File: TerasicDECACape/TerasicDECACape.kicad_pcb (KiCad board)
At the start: 4 copper layers, 54.7 x 66.3 mm, 24 parts, among them CN1 NASB0-S6701-TS50, CN2 NASB0-S6701-TS50, J1 MiSTer SDRAM Module, J2 USB_A, J3 Conn_01x03_Male, M1 Sipeed Lichee, P8 BeagleBone_Black_Header, P9 BeagleBone_Black_Header, SW1 TS-1187A-B-A-B, SW2 TS-1187A-B-A-B

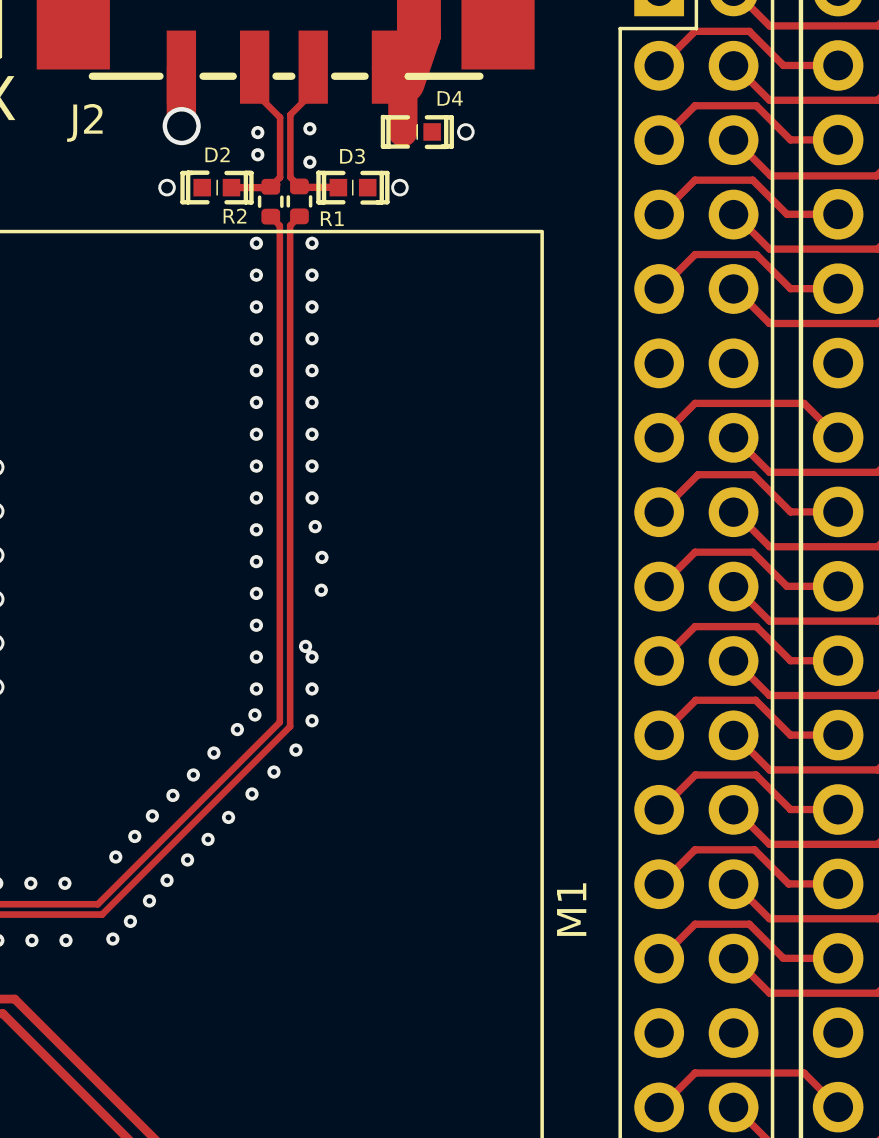
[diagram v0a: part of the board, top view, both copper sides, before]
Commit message: add mounting hole for module
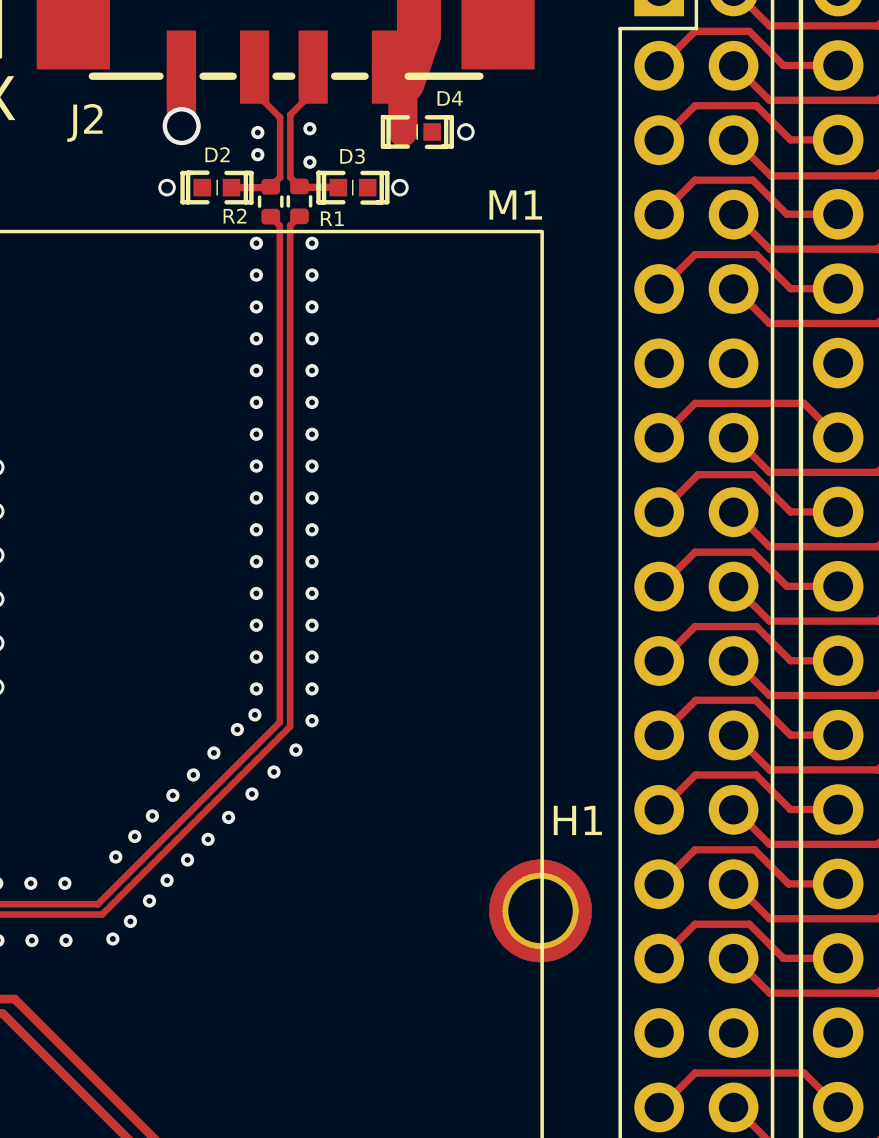
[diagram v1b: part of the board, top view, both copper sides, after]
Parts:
- added H1: MountingHole_Pad, MountingHole:MountingHole_2.2mm_M2_ISO7380_Pad_TopBottom, F.Cu at (154.5, 96.3)
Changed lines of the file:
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@@
     (fp_line (start -2.27 -0.94) (end -2.27 0.94) (layer "F.SilkS") (width 0.15))
     (fp_arc (start 0.001269 0.002199) (mid -0.112199 -0.418731) (end 0 -0.84) (layer "F.SilkS") (width 0.08))
-    (fp_arc (start -0.001269 -0.002199) (mid 0.112199 0.418731) (end 0 0.84) (layer "F.SilkS") (width 0.08))
+    (fp_arc (start -0.001269 -0.002199) (mid 0.112199 0.41873) (end 0 0.84) (layer "F.SilkS") (width 0.08))
     (fp_circle (center -1.6 0.8) (end -1.57 0.8) (layer "F.Fab") (width 0.06) (fill none))
     (pad "1" smd rect locked (at -1.45 0 180) (size 1.19 1.73) (layers "F.Cu" "F.Paste" "F.Mask")
@@
     )
   )
+  (footprint "MountingHole:MountingHole_2.2mm_M2_ISO7380_Pad_TopBottom" (layer "F.Cu")
+    (at 154.4701 96.3224)
+    (descr "Mounting Hole 2.2mm, M2, ISO7380")
+    (tags "mounting hole 2.2mm m2 iso7380")
+    (property "Sheetfile" "TerasicDECACape.kicad_sch")
+    (property "Sheetname" "")
+    (attr exclude_from_pos_files)
+    (fp_text reference "H1" (at 1.27 -3.05) (layer "F.SilkS")
+      (effects (font (size 1 1) (thickness 0.15)))
+    )
+    (fp_text value "MountingHole_Pad" (at 0 2.75) (layer "F.Fab")
+      (effects (font (size 1 1) (thickness 0.15)))
+    )
+    (fp_text user "${REFERENCE}" (at 0 0) (layer "F.Fab")
+      (effects (font (size 1 1) (thickness 0.15)))
+    )
+    (fp_circle (center 0 0) (end 1.75 0) (layer "Cmts.User") (width 0.15) (fill none))
+    (fp_circle (center 0 0) (end 2 0) (layer "F.CrtYd") (width 0.05) (fill none))
+    (pad "1" connect circle (at 0 0) (size 3.5 3.5) (layers "B.Cu" "B.Mask")
+      (net 1 "GND") (pinfunction "1") (pintype "input"))
+    (pad "1" thru_hole circle (at 0 0) (size 2.6 2.6) (drill 2.2) (layers *.Cu *.Mask)
+      (net 1 "GND") (pinfunction "1") (pintype "input"))
+    (pad "1" connect circle (at 0 0) (size 3.5 3.5) (layers "F.Cu" "F.Mask")
+      (net 1 "GND") (pinfunction "1") (pintype "input"))
+  )
   (footprint "easyeda2kicad:Sipeed Lichee" (layer "F.Cu")
     (at 154.5251 96.2324 90)
-    (fp_text reference "M1" (at -0.05 1.045 90 unlocked) (layer "F.SilkS")
+    (fp_text reference "M1" (at 23.97 -0.905 unlocked) (layer "F.SilkS")
       (effects (font (size 1 1) (thickness 0.15)))
     )
@@
   (gr_text "TX" (at 135.2701 68.6324) (layer "F.SilkS")
     (effects (font (size 1.5 1.5) (thickness 0.3)))
+  )
+  (dimension (type aligned) (layer "Dwgs.User")
+    (pts (xy 127.5801 95.0924) (xy 127.5801 96.2624))
+    (height -24.64)
+    (gr_text "1.1700 mm" (at 151.5951 95.6774 90) (layer "Dwgs.User")
+      (effects (font (size 0.5 0.5) (thickness 0.15)))
+    )
+    (format (units 3) (units_format 1) (precision 4))
+    (style (thickness 0.1) (arrow_length 0.5) (text_position_mode 0) (extension_height 0.58642) (extension_offset 0.5) keep_text_aligned)
   )
   (segment (start 126.8501 98.7024) (end 127.5701 97.9824) (width 0.25) (layer "F.Cu") (net 1))
@@
   (via (at 139.8701 97.2824) (size 0.45) (drill 0.2) (layers "F.Cu" "B.Cu") (free) (net 1))
   (via (at 144.7701 88.745724) (size 0.45) (drill 0.2) (layers "F.Cu" "B.Cu") (free) (net 1))
-  (via (at 146.987292 85.375398) (size 0.45) (drill 0.2) (layers "F.Cu" "B.Cu") (free) (net 1))
+  (via (at 146.6701 85.485726) (size 0.45) (drill 0.2) (layers "F.Cu" "B.Cu") (free) (net 1))
   (via (at 124.0701 104.81365) (size 0.45) (drill 0.2) (layers "F.Cu" "B.Cu") (free) (net 1))
   (via (at 144.7701 74.619066) (size 0.45) (drill 0.2) (layers "F.Cu" "B.Cu") (free) (net 1))
@@
   (via (at 124.0701 102.2074) (size 0.45) (drill 0.2) (layers "F.Cu" "B.Cu") (free) (net 1))
   (via (at 141.7201 71.6324) (size 0.6) (drill 0.4) (layers "F.Cu" "B.Cu") (free) (net 1))
-  (via (at 146.449191 87.293844) (size 0.45) (drill 0.2) (layers "F.Cu" "B.Cu") (free) (net 1))
+  (via (at 146.6701 86.572392) (size 0.45) (drill 0.2) (layers "F.Cu" "B.Cu") (free) (net 1))
   (via (at 138.2701 97.3324) (size 0.45) (drill 0.2) (layers "F.Cu" "B.Cu") (free) (net 1))
   (via (at 141.2201 93.0824) (size 0.45) (drill 0.2) (layers "F.Cu" "B.Cu") (free) (net 1))
@@
   (via (at 146.6701 82.225728) (size 0.45) (drill 0.2) (layers "F.Cu" "B.Cu") (free) (net 1))
   (via (at 128.5201 103.5824) (size 0.6) (drill 0.4) (layers "F.Cu" "B.Cu") (net 1))
-  (via (at 146.777194 83.2053) (size 0.45) (drill 0.2) (layers "F.Cu" "B.Cu") (free) (net 1))
+  (via (at 146.6701 83.312394) (size 0.45) (drill 0.2) (layers "F.Cu" "B.Cu") (free) (net 1))
   (via (at 130.1701 118.6824) (size 1.5) (drill 1.2) (layers "F.Cu" "B.Cu") (net 1))
   (via (at 122.2701 105.3824) (size 0.45) (drill 0.2) (layers "F.Cu" "B.Cu") (free) (net 1))
@@
   (via (at 144.7701 81.139062) (size 0.45) (drill 0.2) (layers "F.Cu" "B.Cu") (free) (net 1))
   (via (at 143.1201 93.8824) (size 0.45) (drill 0.2) (layers "F.Cu" "B.Cu") (free) (net 1))
-  (via (at 147.00778 84.255886) (size 0.45) (drill 0.2) (layers "F.Cu" "B.Cu") (free) (net 1))
+  (via (at 146.6701 84.39906) (size 0.45) (drill 0.2) (layers "F.Cu" "B.Cu") (free) (net 1))
   (via (at 122.2701 102.3074) (size 0.45) (drill 0.2) (layers "F.Cu" "B.Cu") (free) (net 1))
   (via (at 122.7201 97.3824) (size 0.45) (drill 0.2) (layers "F.Cu" "B.Cu") (free) (net 1))
@@
   (segment (start 145.5791 69.2394) (end 144.7101 68.3704) (width 0.225) (layer "F.Cu") (net 180))
   (segment (start 145.5791 71.2834) (end 145.5791 69.2394) (width 0.225) (layer "F.Cu") (net 180))
-  (segment (start 145.1701 71.6224) (end 145.3801 71.6224) (width 0.25) (layer "F.Cu") (net 180))
   (segment (start 143.9201 71.6324) (end 145.1601 71.6324) (width 0.25) (layer "F.Cu") (net 180))
   (segment (start 144.7101 68.2824) (end 144.7101 67.5199) (width 0.25) (layer "F.Cu") (net 180))
-  (segment (start 145.3801 71.6224) (end 145.4701 71.5324) (width 0.25) (layer "F.Cu") (net 180))
   (segment (start 144.7101 68.3704) (end 144.7101 67.5199) (width 0.225) (layer "F.Cu") (net 180))
   (segment (start 146.3201 71.6224) (end 147.5601 71.6224) (width 0.25) (layer "F.Cu") (net 181))
   (segment (start 146.7101 68.3424) (end 146.7101 67.5199) (width 0.25) (layer "F.Cu") (net 181))
-  (segment (start 146.1801 71.6224) (end 146.1201 71.6824) (width 0.25) (layer "F.Cu") (net 181))
   (segment (start 146.7101 68.3024) (end 146.7101 67.5199) (width 0.25) (layer "F.Cu") (net 181))
   (segment (start 146.3201 71.6224) (end 146.1801 71.6224) (width 0.25) (layer "F.Cu") (net 181))

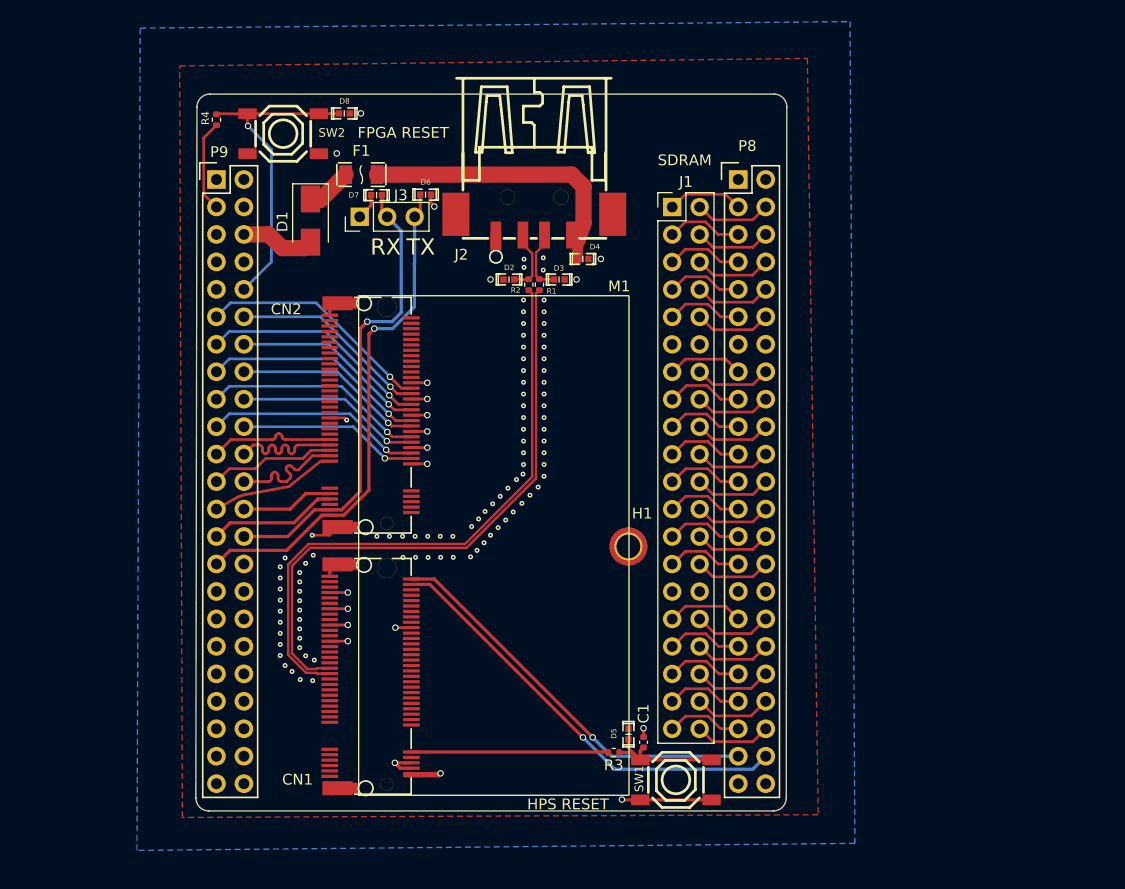
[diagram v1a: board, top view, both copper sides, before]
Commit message: add user IO header, connect UART1 with flow control
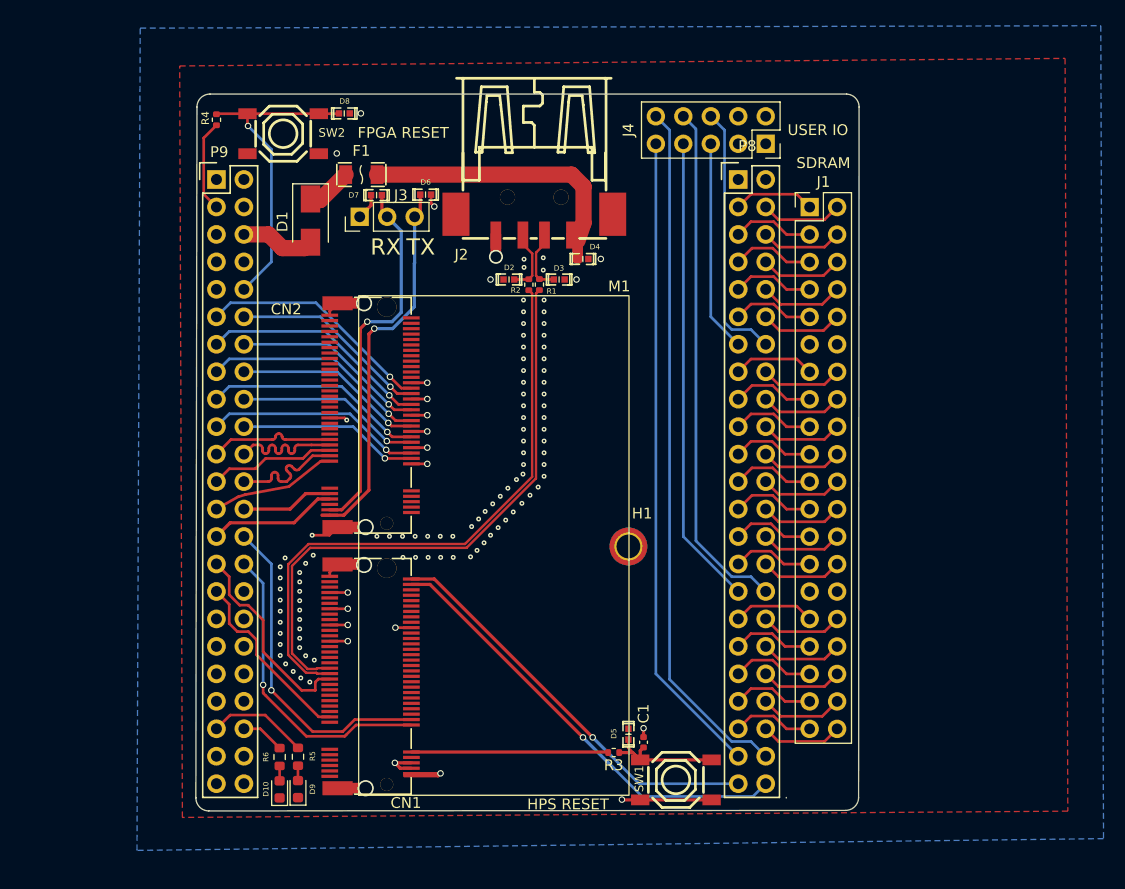
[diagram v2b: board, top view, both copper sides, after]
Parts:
- added D10: red, LED_SMD:LED_0603_1608Metric, F.Cu at (122.2, 118.8)
- added D9: blue, LED_SMD:LED_0603_1608Metric, F.Cu at (123.9, 118.8)
- added J4: Conn_02x05_Odd_Even, Connector_PinSocket_2.54mm:PinSocket_2x05_P2.54mm_Vertical, F.Cu at (167.2, 59.1)
- added R5: 1k, Resistor_SMD:R_0603_1608Metric, F.Cu at (123.9, 115.8)
- added R6: 1k, Resistor_SMD:R_0603_1608Metric, F.Cu at (122.2, 115.8)
- moved J1 12.7 mm to (171.2, 64.9)
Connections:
- CN1 pad 20: /PG8 -> /PG8_UART1_RTS
- CN1 pad 22: /PG9 -> /PG9_UART1_CTS
- CN1 pad 23: /PG7 -> /PG7_UART1_RX
- CN1 pad 37: /PG6 -> /PG6_UART1_TX
- P8 pad 13: unconnected-(P8-Pad13) -> /USER0
- P8 pad 14: unconnected-(P8-Pad14) -> /USER1
- P8 pad 31: unconnected-(P8-Pad31) -> /USER2
- P8 pad 32: unconnected-(P8-Pad32) -> /USER3
- P8 pad 43: /PB10_SCL -> /USER4
- P8 pad 44: /PB11_SDA -> /USER5
- P8 pad 45: unconnected-(P8-Pad45) -> /PB10_SCL
- P8 pad 46: unconnected-(P8-Pad46) -> /PB11_SDA
- P9 pad 28: /PB9_UART0_RX -> /PG9_UART1_CTS
- P9 pad 29: /PB8_UART0_TX -> /PG6_UART1_TX
- P9 pad 30: unconnected-(P9-Pad30) -> /PG8_UART1_RTS
- P9 pad 31: unconnected-(P9-Pad31) -> /PG7_UART1_RX
- P9 pad 41: unconnected-(P9-Pad41) -> /LED1
- P9 pad 42: unconnected-(P9-Pad42) -> /LED2
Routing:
- net /USER5: track 0.00 -> 64.4 mm
- net /USER4: track 0.00 -> 59.8 mm
- net /USER3: track 0.00 -> 48.1 mm
- net /USER2: track 0.00 -> 43.5 mm
- net /PG9_UART1_CTS: track 0.00 -> 30.3 mm, vias 0 -> 1
- net /PG8_UART1_RTS: track 0.00 -> 28.5 mm, vias 0 -> 1
- net /USER1: track 0.00 -> 24.2 mm
- net /USER0: track 0.00 -> 19.6 mm
- net /PG6_UART1_TX: track 0.00 -> 18.9 mm
- net /PG7_UART1_RX: track 0.00 -> 17.1 mm
- net /PB8_UART0_TX: track 47.2 -> 35.6 mm
- net /LED1: track 0.00 -> 9.32 mm
- net /PB9_UART0_RX: track 43.5 -> 34.6 mm
- net /LED2: track 0.00 -> 4.04 mm
- net Net-(R6-Pad1): track 0.00 -> 1.38 mm
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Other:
- board size 54.7 x 66.3 mm -> 61.3 x 66.3 mm
- board text added: "USER IO"

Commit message: fix DRC issues
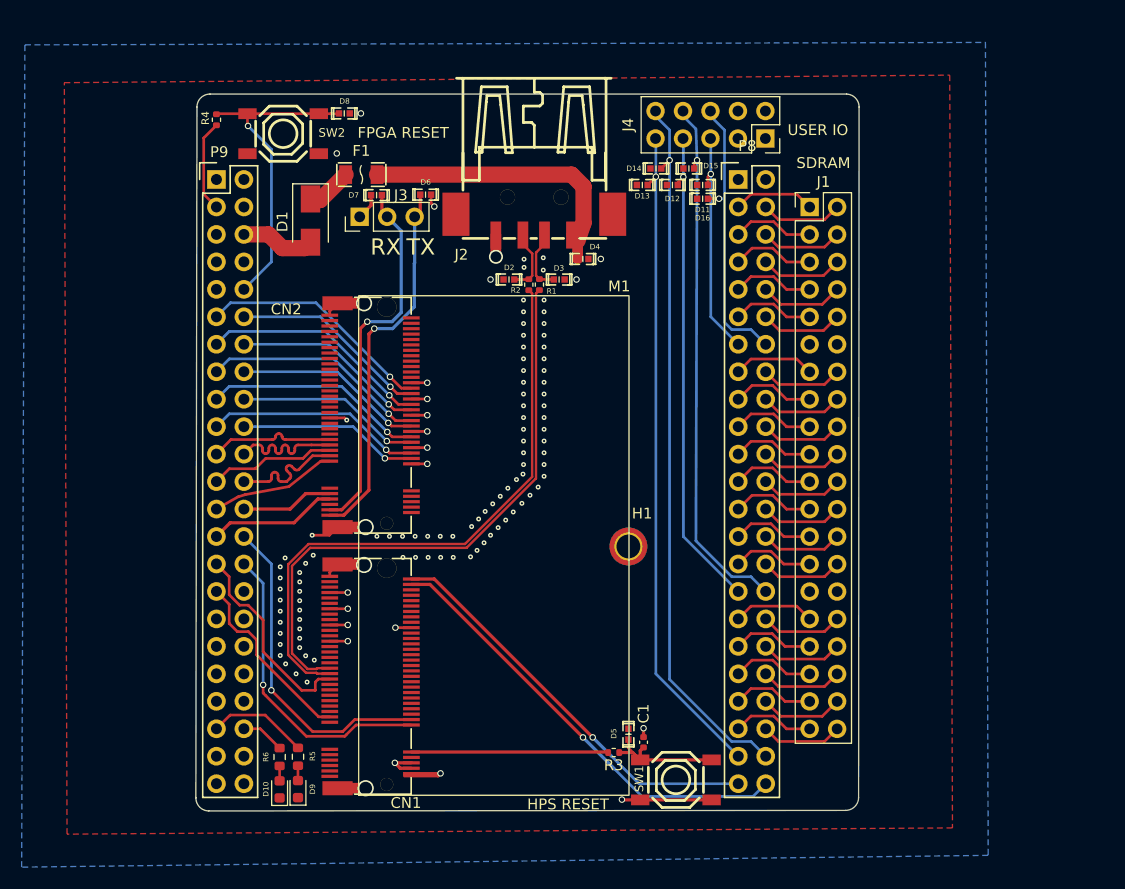
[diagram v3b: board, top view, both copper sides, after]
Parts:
- added D11: LXES15AAA1-133, easyeda2kicad:D0402-BI, F.Cu at (161.3, 62.9)
- added D12: LXES15AAA1-133, easyeda2kicad:D0402-BI, F.Cu at (158.5, 62.9)
- added D13: LXES15AAA1-133, easyeda2kicad:D0402-BI, F.Cu at (155.7, 62.9)
- added D14: LXES15AAA1-133, easyeda2kicad:D0402-BI, F.Cu at (157.0, 61.4)
- added D15: LXES15AAA1-133, easyeda2kicad:D0402-BI, F.Cu at (160.1, 61.4)
- added D16: LXES15AAA1-133, easyeda2kicad:D0402-BI, F.Cu at (161.3, 64.2)
- moved J4 0.49 mm to (167.1, 58.6)
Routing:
- net /USER1: track 24.2 -> 25.8 mm, vias 0 -> 1
- net /USER0: track 19.6 -> 20.7 mm, vias 0 -> 1
- net /USER5: track 64.4 -> 65.5 mm, vias 0 -> 1
- net /USER4: track 59.8 -> 60.9 mm, vias 0 -> 1
- net /USER2: track 43.5 -> 44.5 mm, vias 0 -> 1
- net /USER3: track 48.1 -> 49.0 mm, vias 0 -> 1
- net /PB8_UART0_TX: track 35.6 -> 34.9 mm
- net GND: vias 119 -> 118
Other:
- outline, holes or cut-outs redrawn
